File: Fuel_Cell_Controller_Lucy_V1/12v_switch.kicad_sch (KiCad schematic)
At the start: 5 parts, among them Q2 FMMT491ATA, U12 EL3H7(B)(TA)-VG

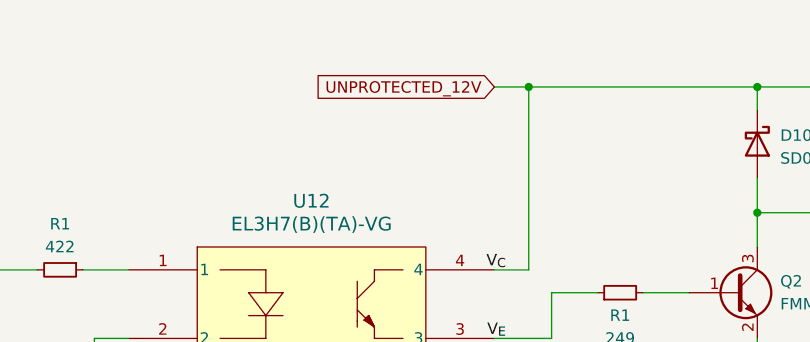
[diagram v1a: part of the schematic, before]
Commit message: Most of the schematic done, pcb layout needs DRC
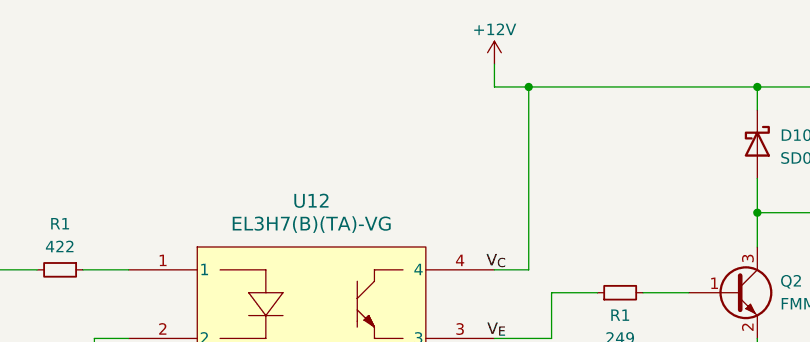
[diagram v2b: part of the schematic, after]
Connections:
- net UNPROTECTED_12V renamed +12V
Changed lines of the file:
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@@
+    (stroke (width 0) (type default))
+  )
+  (wire (pts (xy 152.4 74.93) (xy 152.4 77.47))
     (stroke (width 0) (type default))
   )
@@
   (label "V_{E}" (at 153.67 105.41 180) (fields_autoplaced)
     (effects (font (size 1.27 1.27)) (justify right bottom))
-  )
-  (global_label "UNPROTECTED_12V" (shape input) (at 152.4 77.47 180) (fields_autoplaced)
-    (effects (font (size 1.27 1.27)) (justify right))
-    (property "Intersheetrefs" "${INTERSHEET_REFS}" (at 131.7143 77.47 0)
-      (effects (font (size 1.27 1.27)) (justify right) hide)
-    )
   )
   (hierarchical_label "ENBL_PIN" (shape input) (at 96.52 97.79 180) (fields_autoplaced)
@@
         )
       )
+    )
+  )
+  (symbol (lib_id "power:+12V") (at 152.4 74.93 0) (unit 1)
+    (in_bom yes) (on_board yes) (dnp no) (fields_autoplaced)
+    (property "Reference" "#PWR017" (at 152.4 78.74 0)
+      (effects (font (size 1.27 1.27)) hide)
+    )
+    (property "Value" "+12V" (at 152.4 71.12 0)
+      (effects (font (size 1.27 1.27)))
+    )
+    (property "Footprint" "" (at 152.4 74.93 0)
+      (effects (font (size 1.27 1.27)) hide)
+    )
+    (property "Datasheet" "" (at 152.4 74.93 0)
+      (effects (font (size 1.27 1.27)) hide)
+    )
+    (pin "1")
+    (instances
+      (project "Fuel_Cell_Controller_Prototype"
+        (path "/f651cec9-411c-4a4e-a163-5c49adbe6a12/593c7e68-7c5e-4ef7-bd05-a128c02972b0/03791c1e-c16d-4373-91a4-c197c12e5f34"
+          (reference "#PWR017") (unit 1)
+        )
+        (path "/f651cec9-411c-4a4e-a163-5c49adbe6a12/593c7e68-7c5e-4ef7-bd05-a128c02972b0/4a3d4d32-1493-4777-95d6-a7fe5420f8b8"
+          (reference "#PWR088") (unit 1)
+        )
+      )

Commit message: updated
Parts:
- D10: Part# (none) -> 478-7800-1-ND
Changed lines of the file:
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@@
+      (effects (font (size 1.27 1.27)) hide)
+    )
+    (property "Part#" "478-7800-1-ND" (at 181.61 83.82 0)
       (effects (font (size 1.27 1.27)) hide)
     )

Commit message: lots of changes, pcb ready for order
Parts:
- R1: Part# C2759727 -> dgkey
- R1: Part# C217903 -> dgkey
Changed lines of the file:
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@@
       (effects (font (size 1.27 1.27)) hide)
     )
-    (property "Part#" "C2759727" (at 104.14 97.79 0)
+    (property "Part#" "dgkey" (at 104.14 97.79 0)
       (effects (font (size 1.27 1.27)) hide)
     )
@@
       (effects (font (size 1.27 1.27)) hide)
     )
-    (property "Part#" "C217903" (at 166.37 100.33 0)
+    (property "Part#" "dgkey" (at 166.37 100.33 0)
       (effects (font (size 1.27 1.27)) hide)
     )

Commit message: Started the code
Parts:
- R1: Part# dgkey -> C101033
- R1: Part# dgkey -> C3016229
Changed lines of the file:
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@@
       (effects (font (size 1.27 1.27)) hide)
     )
-    (property "Part#" "dgkey" (at 104.14 97.79 0)
+    (property "Part#" "C101033" (at 104.14 97.79 0)
       (effects (font (size 1.27 1.27)) hide)
     )
@@
       (effects (font (size 1.27 1.27)) hide)
     )
-    (property "Part#" "dgkey" (at 166.37 100.33 0)
+    (property "Part#" "C3016229" (at 166.37 100.33 0)
       (effects (font (size 1.27 1.27)) hide)
     )
